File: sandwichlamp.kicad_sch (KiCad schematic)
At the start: 18 parts, among them J1 Conn_01x01_Pin, J2 Conn_01x01_Pin, J3 Conn_01x01_Pin, J4 12V Enable, J5 HLK-LD2410C, J6 Conn_01x20_Pin, SW1 SW_SPDT, U1 magnetic-charger, U2 esp32-wemos-d1-mini, U3 hw357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

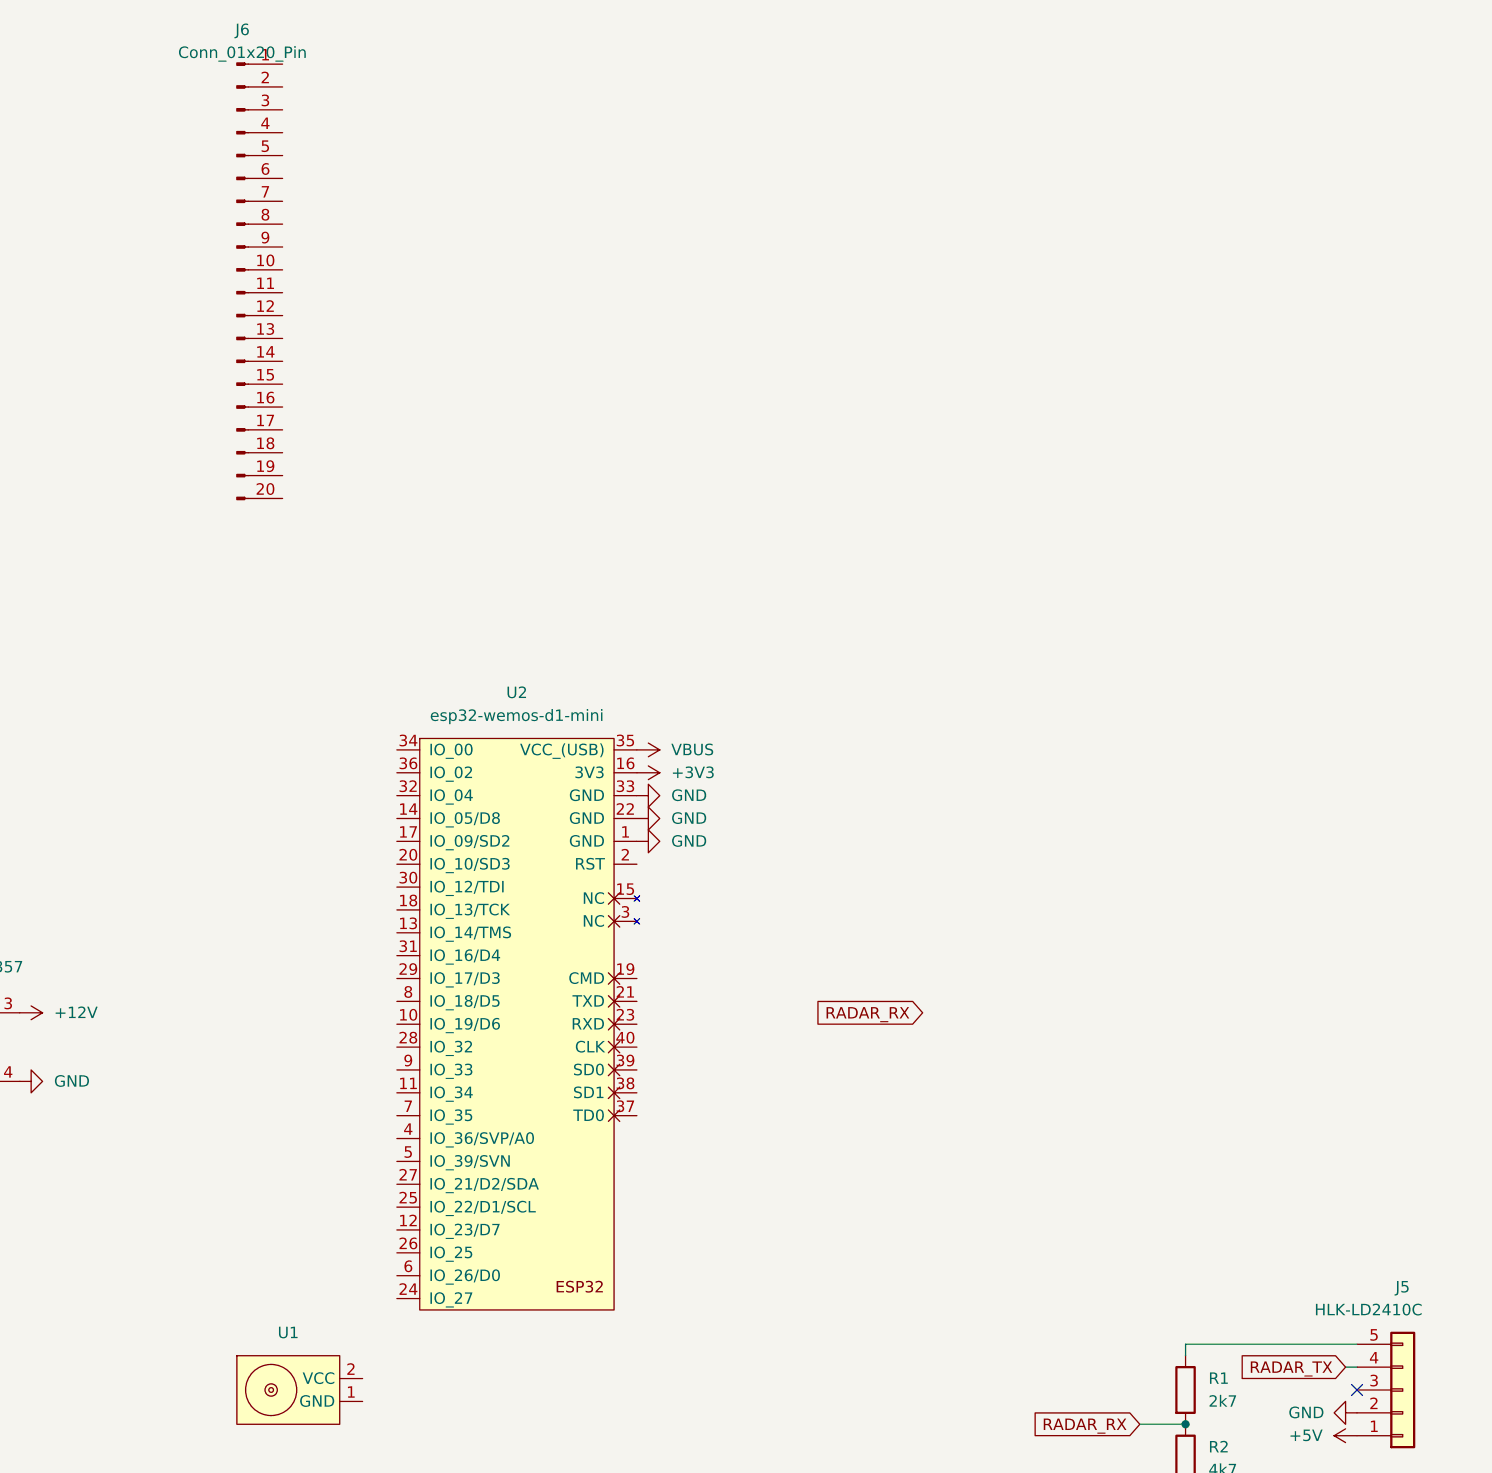
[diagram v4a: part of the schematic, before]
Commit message: Add the new Lolin32 footprint
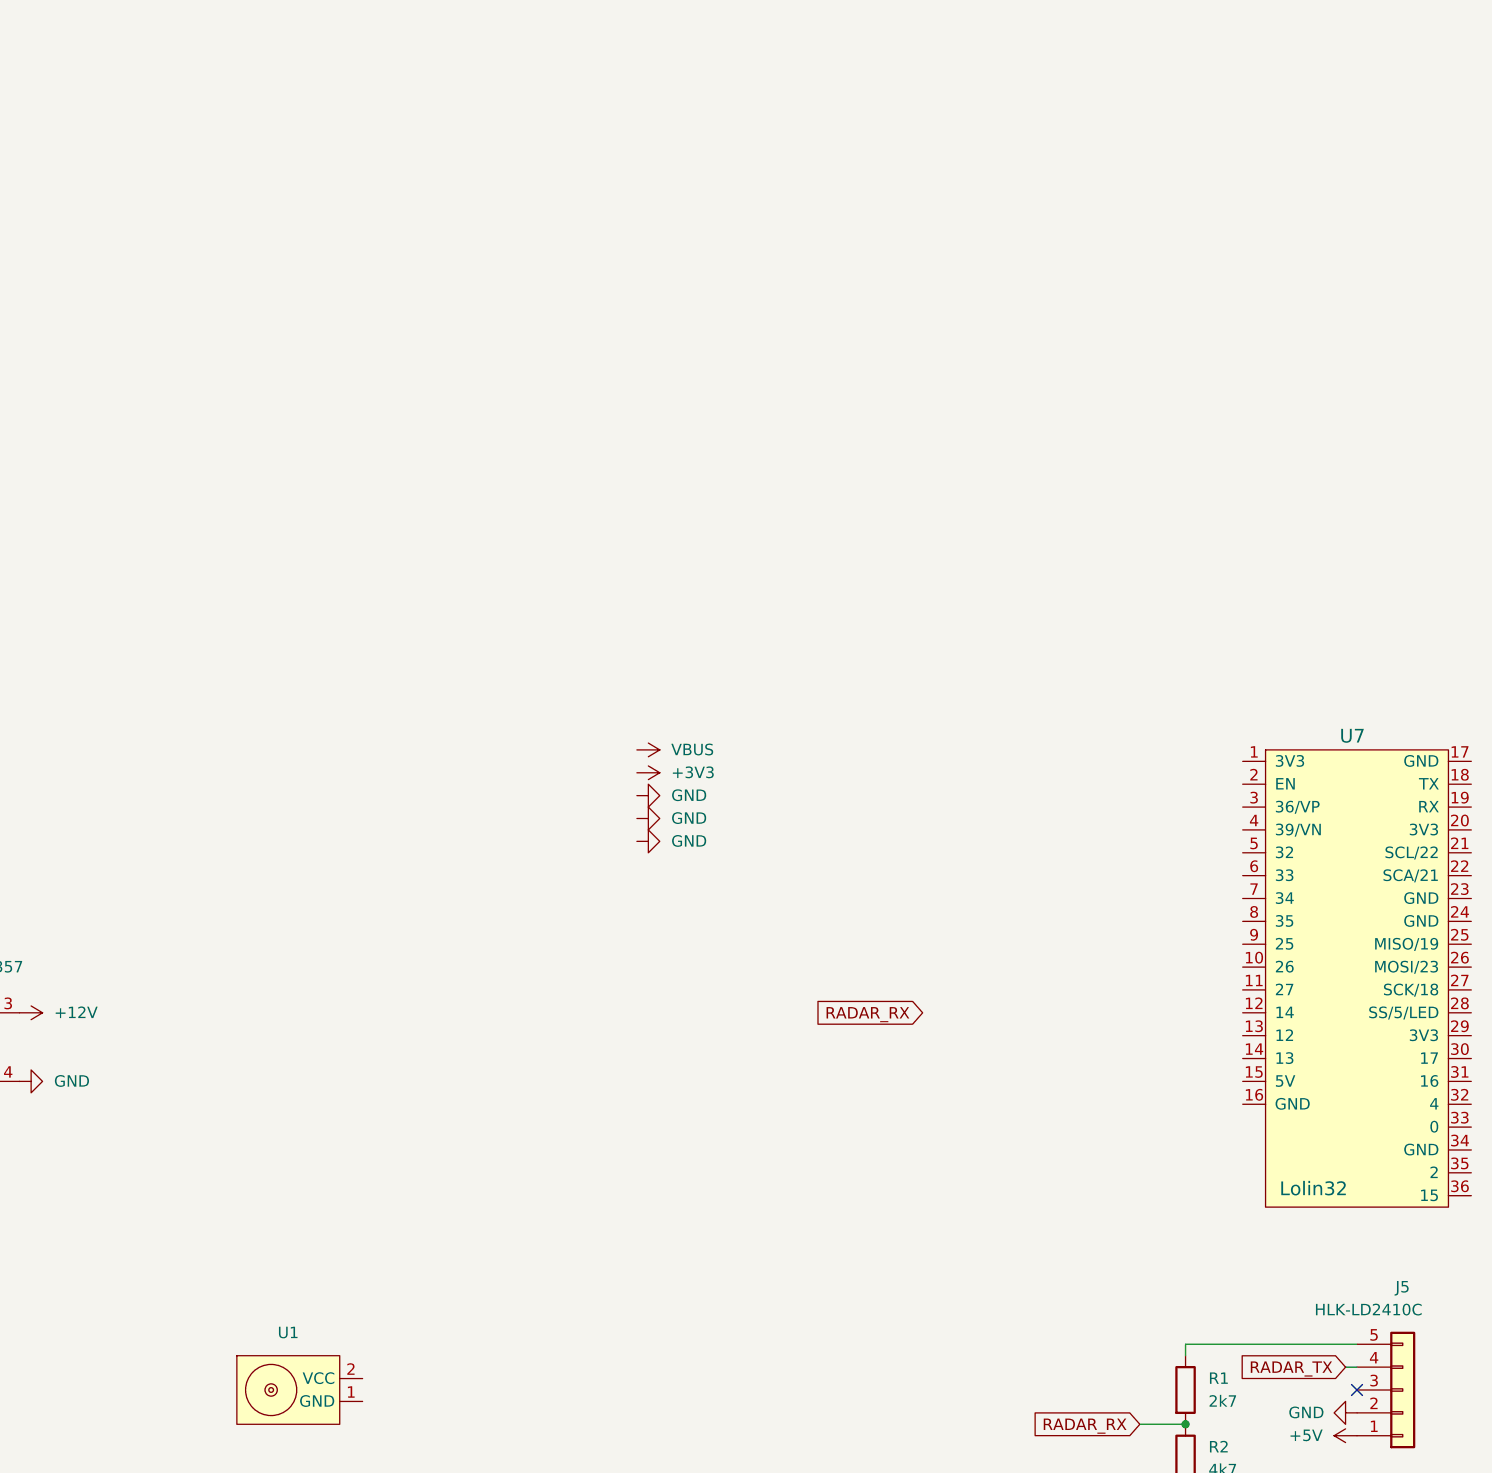
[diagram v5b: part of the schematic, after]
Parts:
- removed J6: Conn_01x20_Pin, Connector_PinHeader_2.54mm:PinHeader_1x20_P2.54mm_Vertical, symbol Connector:Conn_01x20_Pin
- removed U2: esp32-wemos-d1-mini, esp32-wemos-d1-mini:esp32-wemos-d1-mini, symbol esp32-wemos-d1-mini:esp32-wemos-d1-mini
- added U7: Lolin32, lolin32:lolin32, symbol lolin32:lolin32
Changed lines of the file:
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@@
 	)
 	(symbol
-		(lib_id "Connector:Conn_01x20_Pin")
-		(at 107.95 -30.48 0)
-		(unit 1)
-		(exclude_from_sim no)
-		(in_bom yes)
-		(on_board yes)
-		(dnp no)
-		(fields_autoplaced yes)
-		(property "Reference" "J6"
-			(at 108.585 -57.15 0)
-			(effects
-				(font
-					(size 1.27 1.27)
-				)
-			)
-		)
-		(property "Value" "Conn_01x20_Pin"
-			(at 108.585 -54.61 0)
-			(effects
-				(font
-					(size 1.27 1.27)
-				)
-			)
-		)
-		(property "Footprint" "Connector_PinHeader_2.54mm:PinHeader_1x20_P2.54mm_Vertical"
-			(at 107.95 -30.48 0)
-			(effects
-				(font
-					(size 1.27 1.27)
-				)
-				(hide yes)
-			)
-		)
-		(property "Datasheet" "~"
-			(at 107.95 -30.48 0)
-			(effects
-				(font
-					(size 1.27 1.27)
-				)
-				(hide yes)
-			)
-		)
-		(property "Description" "Generic connector, single row, 01x20, script generated"
-			(at 107.95 -30.48 0)
-			(effects
-				(font
-					(size 1.27 1.27)
-				)
-				(hide yes)
-			)
+		(lib_id "lolin32:lolin32")
+		(at 232.41 48.26 0)
+		(unit 1)
+		(exclude_from_sim no)
+		(in_bom yes)
+		(on_board yes)
+		(dnp no)
+		(property "Reference" "U7"
+			(at 231.902 21.336 0)
+			(effects
+				(font
+					(size 1.524 1.524)
+				)
+			)
+		)
+		(property "Value" "Lolin32"
+			(at 227.584 71.628 0)
+			(effects
+				(font
+					(size 1.524 1.524)
+				)
+			)
+		)
+		(property "Footprint" "lolin32:lolin32"
+			(at 232.41 17.78 0)
+			(effects
+				(font
+					(size 1.524 1.524)
+				)
+				(hide yes)
+			)
+		)
+		(property "Datasheet" "https://mischianti.org/esp32-wemos-lolin32-high-resolution-pinout-and-specs/"
+			(at 232.41 20.32 0)
+			(effects
+				(font
+					(size 1.524 1.524)
+				)
+				(hide yes)
+			)
+		)
+		(property "Description" "WeMos Lolin32"
+			(at 230.378 72.136 0)
+			(effects
+				(font
+					(size 1.27 1.27)
+				)
+				(hide yes)
+			)
+		)
+		(pin "15"
+		)
+		(pin "26"
+		)
+		(pin "28"
+		)
+		(pin "27"
+		)
+		(pin "22"
+		)
+		(pin "36"
+		)
+		(pin "23"
+		)
+		(pin "6"
+		)
+		(pin "21"
+		)
+		(pin "29"
+		)
+		(pin "20"
+		)
+		(pin "19"
+		)
+		(pin "2"
+		)
+		(pin "33"
+		)
+		(pin "34"
+		)
+		(pin "11"
+		)
+		(pin "12"
+		)
+		(pin "9"
+		)
+		(pin "13"
+		)
+		(pin "5"
+		)
+		(pin "4"
+		)
+		(pin "10"
+		)
+		(pin "1"
+		)
+		(pin "35"
+		)
+		(pin "17"
+		)
+		(pin "30"
+		)
+		(pin "3"
+		)
+		(pin "7"
+		)
+		(pin "8"
 		)
 		(pin "14"
 		)
-		(pin "6"
-		)
-		(pin "1"
-		)
-		(pin "2"
+		(pin "31"
 		)
 		(pin "18"
 		)
-		(pin "15"
-		)
-		(pin "20"
-		)
-		(pin "4"
-		)
-		(pin "7"
-		)
-		(pin "19"
-		)
-		(pin "10"
-		)
-		(pin "13"
-		)
-		(pin "11"
-		)
-		(pin "3"
-		)
-		(pin "5"
-		)
 		(pin "16"
 		)
-		(pin "12"
-		)
-		(pin "17"
-		)
-		(pin "8"
-		)
-		(pin "9"
+		(pin "32"
+		)
+		(pin "24"
+		)
+		(pin "25"
 		)
 		(instances
 			(project ""
 				(path "/e0ec050d-3d79-41e4-bfa7-38c68df5e8aa"
-					(reference "J6")
+					(reference "U7")
 					(unit 1)
 				)
@@
 					(unit 1)
 				)
-			)
-		)
-	)
-	(symbol
-		(lib_id "esp32-wemos-d1-mini:esp32-wemos-d1-mini")
-		(at 138.43 20.32 0)
-		(unit 1)
-		(exclude_from_sim no)
-		(in_bom yes)
-		(on_board yes)
-		(dnp no)
-		(fields_autoplaced yes)
-		(property "Reference" "U2"
-			(at 139.065 16.51 0)
-			(effects
-				(font
-					(size 1.27 1.27)
-				)
-			)
-		)
-		(property "Value" "esp32-wemos-d1-mini"
-			(at 139.065 19.05 0)
-			(effects
-				(font
-					(size 1.27 1.27)
-				)
-			)
-		)
-		(property "Footprint" "esp32-wemos-d1-mini:esp32-wemos-d1-mini"
-			(at 142.24 17.78 0)
-			(effects
-				(font
-					(size 1.27 1.27)
-				)
-				(hide yes)
-			)
-		)
-		(property "Datasheet" ""
-			(at 142.24 17.78 0)
-			(effects
-				(font
-					(size 1.27 1.27)
-				)
-				(hide yes)
-			)
-		)
-		(property "Description" ""
-			(at 138.43 20.32 0)
-			(effects
-				(font
-					(size 1.27 1.27)
-				)
-				(hide yes)
-			)
-		)
-		(pin "9"
-		)
-		(pin "17"
-		)
-		(pin "1"
-		)
-		(pin "3"
-		)
-		(pin "18"
-		)
-		(pin "10"
-		)
-		(pin "23"
-		)
-		(pin "26"
-		)
-		(pin "27"
-		)
-		(pin "29"
-		)
-		(pin "33"
-		)
-		(pin "35"
-		)
-		(pin "11"
-		)
-		(pin "5"
-		)
-		(pin "12"
-		)
-		(pin "20"
-		)
-		(pin "21"
-		)
-		(pin "32"
-		)
-		(pin "2"
-		)
-		(pin "4"
-		)
-		(pin "15"
-		)
-		(pin "16"
-		)
-		(pin "22"
-		)
-		(pin "30"
-		)
-		(pin "28"
-		)
-		(pin "31"
-		)
-		(pin "37"
-		)
-		(pin "38"
-		)
-		(pin "6"
-		)
-		(pin "7"
-		)
-		(pin "25"
-		)
-		(pin "19"
-		)
-		(pin "24"
-		)
-		(pin "13"
-		)
-		(pin "40"
-		)
-		(pin "8"
-		)
-		(pin "14"
-		)
-		(pin "34"
-		)
-		(pin "39"
-		)
-		(pin "36"
-		)
-		(instances
-			(project ""
-				(path "/e0ec050d-3d79-41e4-bfa7-38c68df5e8aa"
-					(reference "U2")
-					(unit 1)
-				)

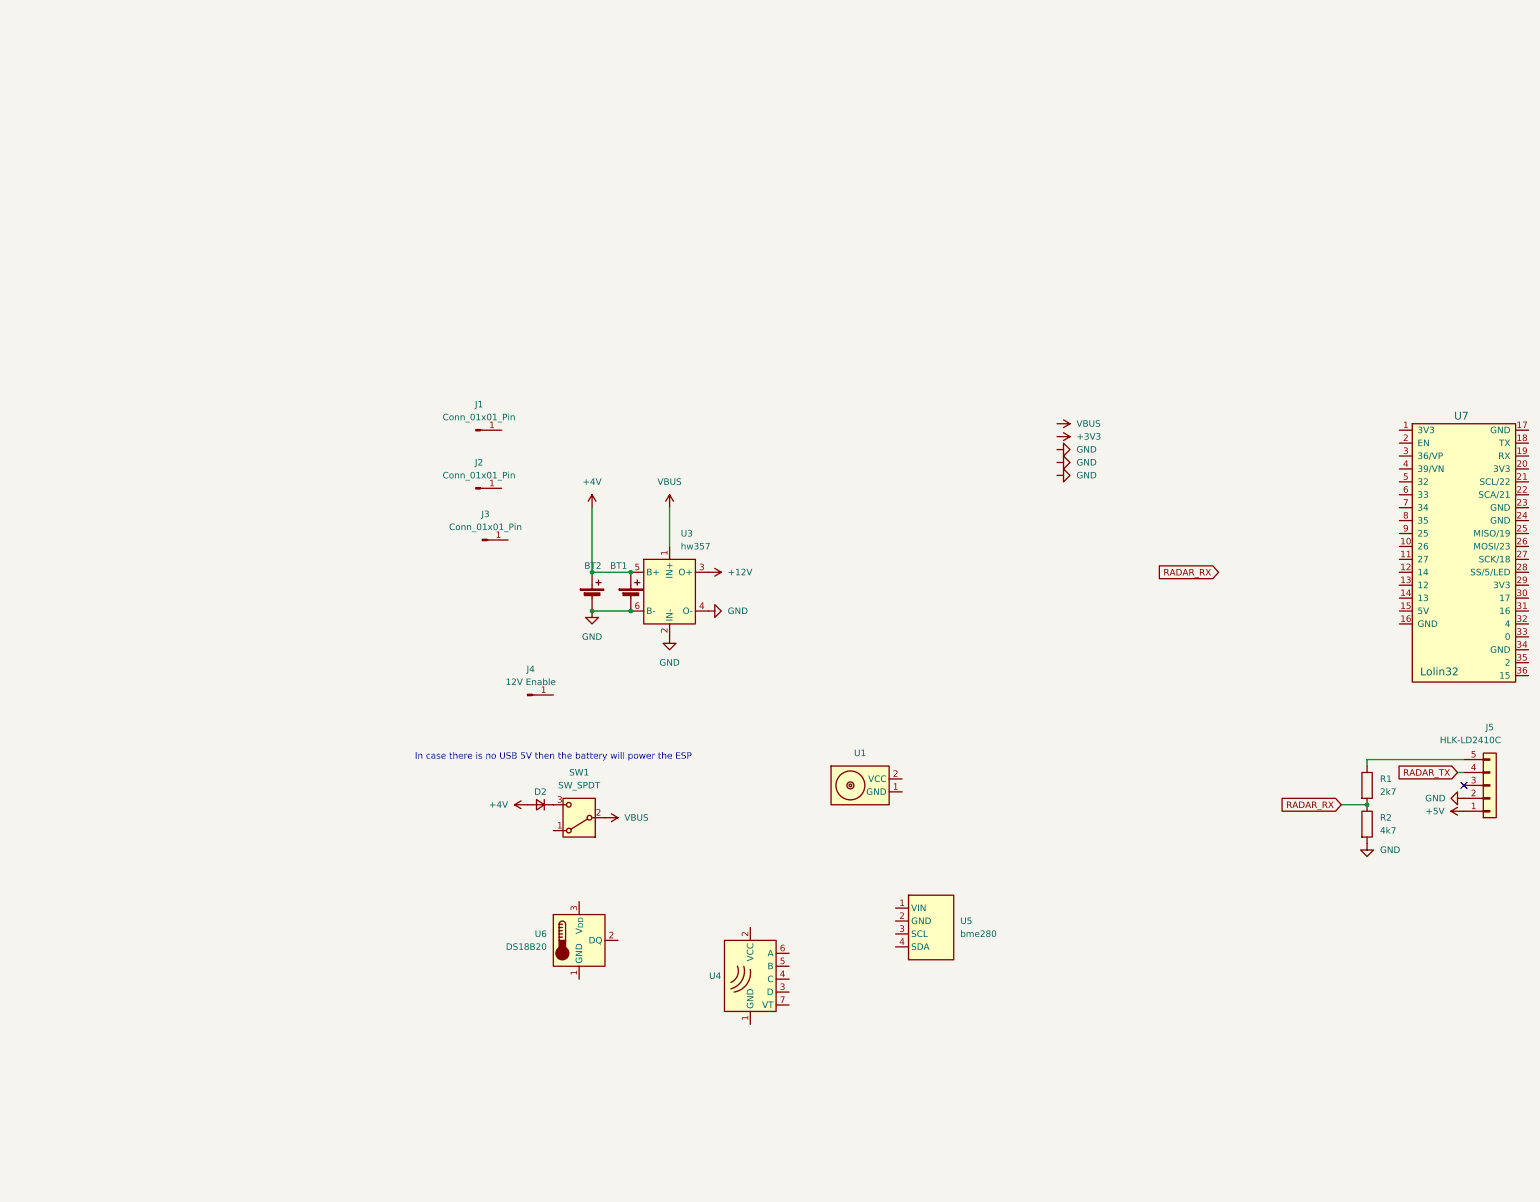
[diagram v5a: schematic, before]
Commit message: Add power switch and power switch for the radar
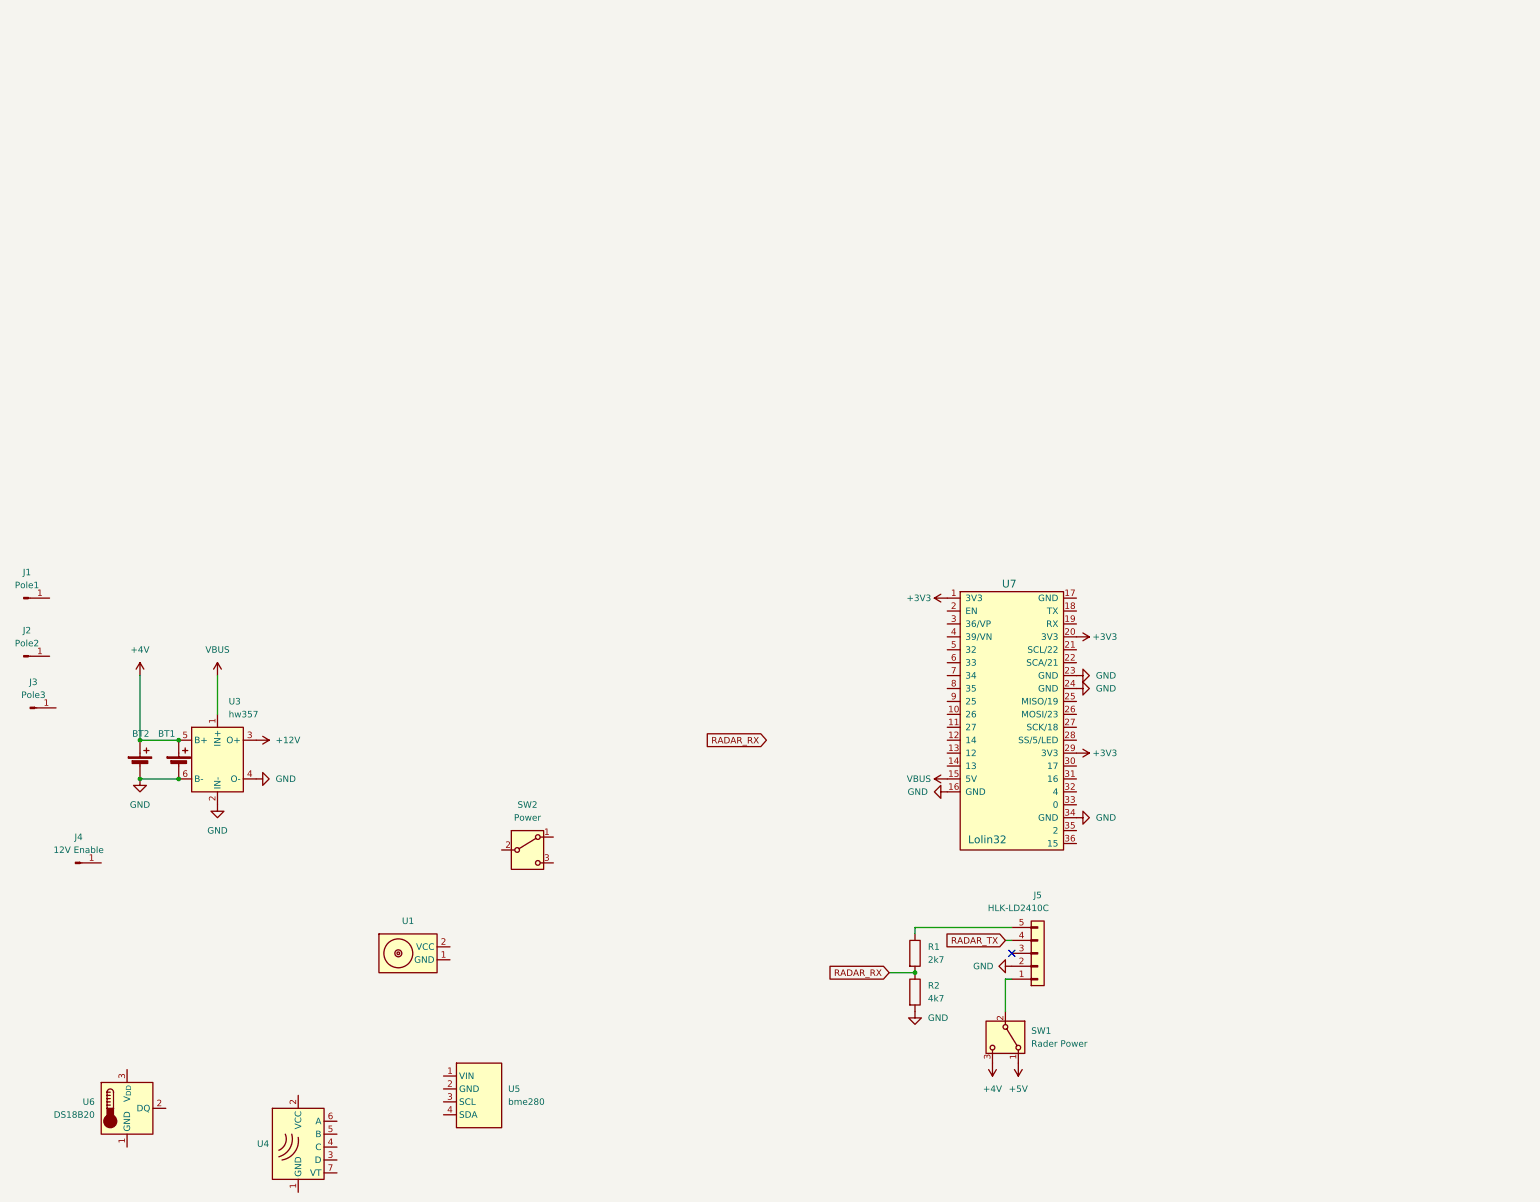
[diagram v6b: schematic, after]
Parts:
- removed D2: D_Small, symbol Device:D_Small
- added SW2: Power, Connector_PinHeader_2.54mm:PinHeader_1x03_P2.54mm_Vertical, symbol Switch:SW_SPDT
- J1: value Conn_01x01_Pin -> Pole1; footprint MountingHole:MountingHole_6.4mm_M6_DIN965_Pad -> MountingHole:MountingHole_4.3mm_M4_ISO7380_Pad_TopOnly
- J2: value Conn_01x01_Pin -> Pole2
- J3: value Conn_01x01_Pin -> Pole3
- SW1: value SW_SPDT -> Rader Power
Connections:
- net +3V3: now also U7.1 (3V3), U7.20 (3V3), U7.29 (3V3)
- net +4V: now also SW1.3 (C)
- net +5V: now also SW1.1 (A); no longer J5.1 (Pin_1)
- net GND: now also U7.16 (GND), U7.23 (GND), U7.24 (GND), U7.34 (GND)
- net VBUS: now also U7.15 (5V); no longer SW1.2 (B)
- new net: J5.1 (Pin_1), SW1.2 (B)
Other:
- note removed: "In case there is no USB 5V then the battery will power the ESP"
- moved on the sheet: BT1, BT2, J1, J2, J3, J4, J5, R1, R2, SW1, U1, U3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
